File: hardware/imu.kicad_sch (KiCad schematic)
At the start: 0 parts

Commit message: wip: schematic sheets in progress
Co-Authored-By: Claude Opus 5.5 <noreply@anthropic.com>
Claude-Session: https://claude.ai/code/session_01RFaS5jnC9tnPam9GBgmGnG
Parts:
- added C61, C62: 1uF, lib:C_0201_0603Metric_W, symbol Device:C
- added R49: 10k, lib:R_0201_0603Metric_W, symbol Device:R
- added U11: BMI270, lib:LGA-14_L3.0-W2.5-P0.50-BR_W, symbol OpenDrone:BMI270
- added U12: TPS7A2018, lib:X2SON-4_L1.0-W1.0-P0.65-TL-EP_Dense, symbol lib:TPS7A2018PDQN
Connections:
- new net +1V8: C62.1, U11.8 (VDD), U12.1 (OUT)
- new net +3V3: C61.1, R49.2, U11.5 (VDDIO), U12.3 (EN), U12.4 (IN)
- new net GND: C61.2, C62.2, U11.6 (GNDIO), U11.7 (GND), U12.2 (GND), U12.5 (EP)
- new net GYRO_CLKIN: U11.9 (INT2)
- new net GYRO_CS: R49.1, U11.12 (CSB)
- new net GYRO_INT: U11.4 (INT1)
- new net SPI1_MISO: U11.1 (SDO)
- new net SPI1_MOSI: U11.14 (SDx)
- new net SPI1_SCK: U11.13 (SCx)
- no-connect marks 0 -> 4
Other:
- note added: "Universal IMU wiring and LGA-14 land (BMI270, ICM-42688-P)"

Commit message: wip: schematic integration in progress (saved after container restart)
Co-Authored-By: Claude Opus 5.5 <noreply@anthropic.com>
Claude-Session: https://claude.ai/code/session_01RFaS5jnC9tnPam9GBgmGnG
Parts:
- U11: symbol OpenDrone:BMI270 -> lib:BMI270
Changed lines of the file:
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@@
 		(in_pos_files no)
 		(dnp no)
-		(property "Reference" "#PWR01"
+		(property "Reference" "#PWR130"
 			(at 83.82 46.99 0)
 			(hide yes)
@@
 			(project "OpenAIO-Whoop"
 				(path "/2c3a7206-1e66-4d43-a02f-491225e20dd6/f446158c-b285-51eb-bc17-5ec1fb190fc1"
-					(reference "#PWR01")
+					(reference "#PWR130")
 					(unit 1)
 				)
@@
 		(in_pos_files no)
 		(dnp no)
-		(property "Reference" "#PWR07"
+		(property "Reference" "#PWR128"
 			(at 26.67 46.99 0)
 			(hide yes)
@@
 			(project "OpenAIO-Whoop"
 				(path "/2c3a7206-1e66-4d43-a02f-491225e20dd6/f446158c-b285-51eb-bc17-5ec1fb190fc1"
-					(reference "#PWR07")
+					(reference "#PWR128")
 					(unit 1)
 				)
@@
 	)
 	(symbol
-		(lib_id "OpenDrone:BMI270")
+		(lib_id "lib:BMI270")
 		(at 72.39 69.85 0)
 		(unit 1)
@@
 		(in_pos_files no)
 		(dnp no)
-		(property "Reference" "#PWR08"
+		(property "Reference" "#PWR133"
 			(at 41.91 62.23 0)
 			(hide yes)
@@
 			(project "OpenAIO-Whoop"
 				(path "/2c3a7206-1e66-4d43-a02f-491225e20dd6/f446158c-b285-51eb-bc17-5ec1fb190fc1"
-					(reference "#PWR08")
+					(reference "#PWR133")
 					(unit 1)
 				)
@@
 		(in_pos_files no)
 		(dnp no)
-		(property "Reference" "#PWR05"
+		(property "Reference" "#PWR135"
 			(at 72.39 99.06 0)
 			(hide yes)
@@
 			(project "OpenAIO-Whoop"
 				(path "/2c3a7206-1e66-4d43-a02f-491225e20dd6/f446158c-b285-51eb-bc17-5ec1fb190fc1"
-					(reference "#PWR05")
+					(reference "#PWR135")
 					(unit 1)
 				)
@@
 		(in_pos_files no)
 		(dnp no)
-		(property "Reference" "#PWR02"
+		(property "Reference" "#PWR132"
 			(at 83.82 57.15 0)
 			(hide yes)
@@
 			(project "OpenAIO-Whoop"
 				(path "/2c3a7206-1e66-4d43-a02f-491225e20dd6/f446158c-b285-51eb-bc17-5ec1fb190fc1"
-					(reference "#PWR02")
+					(reference "#PWR132")
 					(unit 1)
 				)
@@
 		(in_pos_files no)
 		(dnp no)
-		(property "Reference" "#PWR04"
+		(property "Reference" "#PWR131"
 			(at 62.23 57.15 0)
 			(hide yes)
@@
 			(project "OpenAIO-Whoop"
 				(path "/2c3a7206-1e66-4d43-a02f-491225e20dd6/f446158c-b285-51eb-bc17-5ec1fb190fc1"
-					(reference "#PWR04")
+					(reference "#PWR131")
 					(unit 1)
 				)
@@
 		(in_pos_files no)
 		(dnp no)
-		(property "Reference" "#PWR06"
+		(property "Reference" "#PWR134"
 			(at 116.84 82.55 0)
 			(hide yes)
@@
 			(project "OpenAIO-Whoop"
 				(path "/2c3a7206-1e66-4d43-a02f-491225e20dd6/f446158c-b285-51eb-bc17-5ec1fb190fc1"
-					(reference "#PWR06")
+					(reference "#PWR134")
 					(unit 1)
 				)
@@
 		(in_pos_files no)
 		(dnp no)
-		(property "Reference" "#PWR03"
+		(property "Reference" "#PWR129"
 			(at 62.23 46.99 0)
 			(hide yes)
@@
 			(project "OpenAIO-Whoop"
 				(path "/2c3a7206-1e66-4d43-a02f-491225e20dd6/f446158c-b285-51eb-bc17-5ec1fb190fc1"
-					(reference "#PWR03")
-					(unit 1)
-				)
+					(reference "#PWR129")
+					(unit 1)
+				)

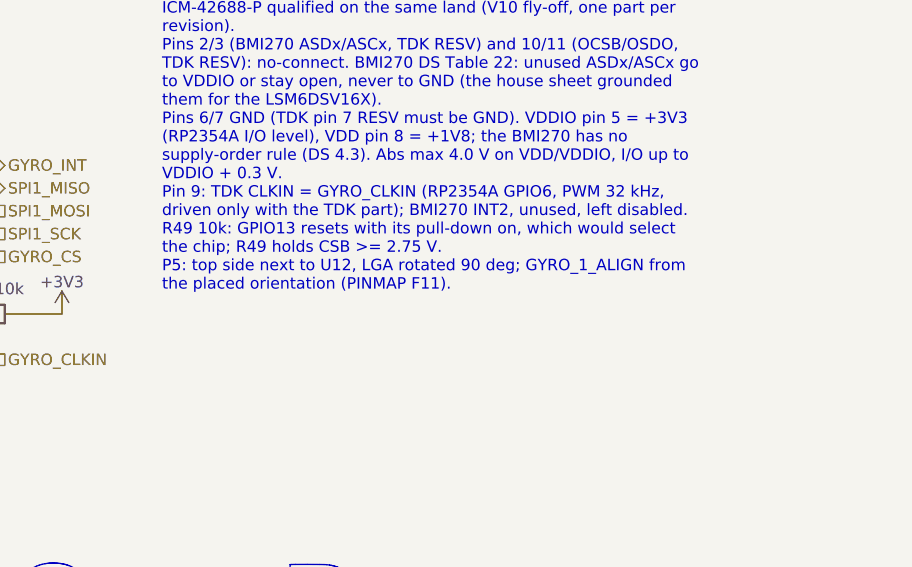
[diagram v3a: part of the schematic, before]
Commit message: wip: routing prep (zones and via fields) and schematic review round 4
Co-Authored-By: Claude Opus 5.5 <noreply@anthropic.com>
Claude-Session: https://claude.ai/code/session_01RFaS5jnC9tnPam9GBgmGnG
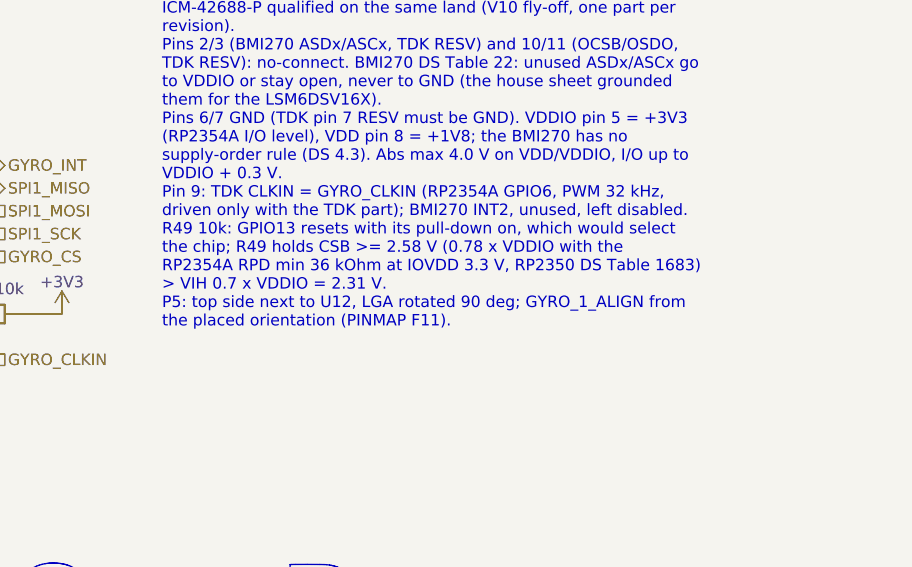
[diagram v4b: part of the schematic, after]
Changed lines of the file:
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@@
 		)
 	)
-	(text_box "GYRO BMI270: U11, R49\nSource: OpenFC-Lite-Mini imu.kicad_sch (universal LGA-14 land, SPI1 4-wire, R49), copied and adapted. BMI270 on the BOM; TDK ICM-42688-P qualified on the same land (V10 fly-off, one part per revision).\nPins 2/3 (BMI270 ASDx/ASCx, TDK RESV) and 10/11 (OCSB/OSDO, TDK RESV): no-connect. BMI270 DS Table 22: unused ASDx/ASCx go to VDDIO or stay open, never to GND (the house sheet grounded them for the LSM6DSV16X).\nPins 6/7 GND (TDK pin 7 RESV must be GND). VDDIO pin 5 = +3V3 (RP2354A I/O level), VDD pin 8 = +1V8; the BMI270 has no supply-order rule (DS 4.3). Abs max 4.0 V on VDD/VDDIO, I/O up to VDDIO + 0.3 V.\nPin 9: TDK CLKIN = GYRO_CLKIN (RP2354A GPIO6, PWM 32 kHz, driven only with the TDK part); BMI270 INT2, unused, left disabled.\nR49 10k: GPIO13 resets with its pull-down on, which would select the chip; R49 holds CSB >= 2.75 V.\nP5: top side next to U12, LGA rotated 90 deg; GYRO_1_ALIGN from the placed orientation (PINMAP F11)."
+	(text_box "GYRO BMI270: U11, R49\nSource: OpenFC-Lite-Mini imu.kicad_sch (universal LGA-14 land, SPI1 4-wire, R49), copied and adapted. BMI270 on the BOM; TDK ICM-42688-P qualified on the same land (V10 fly-off, one part per revision).\nPins 2/3 (BMI270 ASDx/ASCx, TDK RESV) and 10/11 (OCSB/OSDO, TDK RESV): no-connect. BMI270 DS Table 22: unused ASDx/ASCx go to VDDIO or stay open, never to GND (the house sheet grounded them for the LSM6DSV16X).\nPins 6/7 GND (TDK pin 7 RESV must be GND). VDDIO pin 5 = +3V3 (RP2354A I/O level), VDD pin 8 = +1V8; the BMI270 has no supply-order rule (DS 4.3). Abs max 4.0 V on VDD/VDDIO, I/O up to VDDIO + 0.3 V.\nPin 9: TDK CLKIN = GYRO_CLKIN (RP2354A GPIO6, PWM 32 kHz, driven only with the TDK part); BMI270 INT2, unused, left disabled.\nR49 10k: GPIO13 resets with its pull-down on, which would select the chip; R49 holds CSB >= 2.58 V (0.78 x VDDIO with the RP2354A RPD min 36 kOhm at IOVDD 3.3 V, RP2350 DS Table 1683) > VIH 0.7 x VDDIO = 2.31 V.\nP5: top side next to U12, LGA rotated 90 deg; GYRO_1_ALIGN from the placed orientation (PINMAP F11)."
 		(exclude_from_sim no)
 		(at 127 36.83 0)

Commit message: WIP final schematic (D111/D113): GPIO map, D100 oscillator, final footprints, lineup power-net names; mid-run snapshot, not yet verified (ERC/netlist/DRU regen pending)
Co-Authored-By: Claude Opus 5.5 <noreply@anthropic.com>
Claude-Session: https://claude.ai/code/session_01RFaS5jnC9tnPam9GBgmGnG
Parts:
- C61, C62: footprint lib:C_0201_0603Metric_W -> lib:C_0201_0603Metric_L
- R49: footprint lib:R_0201_0603Metric_W -> lib:R_0201_0603Metric_L
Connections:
- net +1V8 renamed +1.8V_GYRO
- net +3V3 renamed +3.3V
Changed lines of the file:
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@@
 		)
 	)
-	(text_box "GYRO BMI270: U11, R49\nSource: OpenFC-Lite-Mini imu.kicad_sch (universal LGA-14 land, SPI1 4-wire, R49), copied and adapted. BMI270 on the BOM; TDK ICM-42688-P qualified on the same land (V10 fly-off, one part per revision).\nPins 2/3 (BMI270 ASDx/ASCx, TDK RESV) and 10/11 (OCSB/OSDO, TDK RESV): no-connect. BMI270 DS Table 22: unused ASDx/ASCx go to VDDIO or stay open, never to GND (the house sheet grounded them for the LSM6DSV16X).\nPins 6/7 GND (TDK pin 7 RESV must be GND). VDDIO pin 5 = +3V3 (RP2354A I/O level), VDD pin 8 = +1V8; the BMI270 has no supply-order rule (DS 4.3). Abs max 4.0 V on VDD/VDDIO, I/O up to VDDIO + 0.3 V.\nPin 9: TDK CLKIN = GYRO_CLKIN (RP2354A GPIO6, PWM 32 kHz, driven only with the TDK part); BMI270 INT2, unused, left disabled.\nR49 10k: GPIO13 resets with its pull-down on, which would select the chip; R49 holds CSB >= 2.58 V (0.78 x VDDIO with the RP2354A RPD min 36 kOhm at IOVDD 3.3 V, RP2350 DS Table 1683) > VIH 0.7 x VDDIO = 2.31 V.\nP5: top side next to U12, LGA rotated 90 deg; GYRO_1_ALIGN from the placed orientation (PINMAP F11)."
+	(text_box "GYRO BMI270: U11, R49\nSource: OpenFC-Lite-Mini imu.kicad_sch (universal LGA-14 land, SPI1 4-wire, R49), copied and adapted. BMI270 on the BOM; TDK ICM-42688-P qualified on the same land (V10 fly-off, one part per revision).\nPins 2/3 (BMI270 ASDx/ASCx, TDK RESV) and 10/11 (OCSB/OSDO, TDK RESV): no-connect. BMI270 DS Table 22: unused ASDx/ASCx go to VDDIO or stay open, never to GND (the house sheet grounded them for the LSM6DSV16X).\nPins 6/7 GND (TDK pin 7 RESV must be GND). VDDIO pin 5 = +3.3V (RP2354A I/O level), VDD pin 8 = +1.8V_GYRO; the BMI270 has no supply-order rule (DS 4.3). Abs max 4.0 V on VDD/VDDIO, I/O up to VDDIO + 0.3 V.\nPin 9: TDK CLKIN = GYRO_CLKIN (RP2354A GPIO6, PWM 32 kHz, driven only with the TDK part); BMI270 INT2, unused, left disabled.\nR49 10k: GPIO13 resets with its pull-down on, which would select the chip; R49 holds CSB >= 2.58 V (0.78 x VDDIO with the RP2354A RPD min 36 kOhm at IOVDD 3.3 V, RP2350 DS Table 1683) > VIH 0.7 x VDDIO = 2.31 V.\nP5: top side next to U12, LGA rotated 90 deg; GYRO_1_ALIGN from the placed orientation (PINMAP F11)."
 		(exclude_from_sim no)
 		(at 127 36.83 0)
@@
 		)
 	)
-	(text_box "+1V8 GYRO LDO: U12, C61, C62 (D52 BR-09, P4-17)\nSource: pcb-agent-commons blocks/LDO_IMU_TPS7A2033 (OpenFC-H7) topology with the 1.8 V part and no ferrite (fed from the +3V3 LDO); the house OpenFC-Lite-Mini also runs the gyro VDD from its own 1.8 V LDO.\nTPS7A2018 DQN: 1 OUT, 2 GND, 3 EN, 4 IN, 5 EP to GND. IN = EN = +3V3: VIN 1.6-6.0 V, VEN 0-6.0 V (abs max 6.5 V), EN never above IN. Load < 1 mA.\nNo 100 nF at the gyro: C61 = U12 CIN at BMI270 VDDIO pin 5, C62 = U12 COUT at VDD pin 8 (COUT >= 0.47 uF effective, ESR <= 100 mOhm: about 0.6-0.85 uF at 1.8 V). C61 counts in the +3V3 COUT sum (P4-12, POWER).\nP5: U12 on the gyro side with OUT facing pin 8; C61 between U12 pin 4 and gyro pin 5, C62 <= 1.5 mm from pin 8 (PS-06), else re-place U12."
+	(text_box "+1.8V_GYRO GYRO LDO: U12, C61, C62 (D52 BR-09, P4-17)\nSource: pcb-agent-commons blocks/LDO_IMU_TPS7A2033 (OpenFC-H7) topology with the 1.8 V part and no ferrite (fed from the +3.3V LDO); the house OpenFC-Lite-Mini also runs the gyro VDD from its own 1.8 V LDO.\nTPS7A2018 DQN: 1 OUT, 2 GND, 3 EN, 4 IN, 5 EP to GND. IN = EN = +3.3V: VIN 1.6-6.0 V, VEN 0-6.0 V (abs max 6.5 V), EN never above IN. Load < 1 mA.\nNo 100 nF at the gyro: C61 = U12 CIN at BMI270 VDDIO pin 5, C62 = U12 COUT at VDD pin 8 (COUT >= 0.47 uF effective, ESR <= 100 mOhm: about 0.6-0.85 uF at 1.8 V). C61 counts in the +3.3V COUT sum (P4-12, POWER).\nP5: U12 on the gyro side with OUT facing pin 8; C61 between U12 pin 4 and gyro pin 5, C62 <= 1.5 mm from pin 8 (PS-06), else re-place U12."
 		(exclude_from_sim no)
 		(at 12.7 99.06 0)
@@
 	)
 	(symbol
-		(lib_id "power:+3V3")
+		(lib_id "power:+3.3V")
 		(at 83.82 43.18 0)
 		(unit 1)
@@
 		(in_pos_files no)
 		(dnp no)
-		(property "Reference" "#PWR135"
+		(property "Reference" "#PWR136"
 			(at 83.82 46.99 0)
 			(hide yes)
@@
 			)
 		)
-		(property "Value" "+3V3"
+		(property "Value" "+3.3V"
 			(at 83.82 39.624 0)
 			(show_name no)
@@
 			)
 		)
-		(property "Description" "Power symbol creates a global label with name \"+3V3\""
+		(property "Description" "Power symbol creates a global label with name \"+3.3V\""
 			(at 83.82 43.18 0)
 			(hide yes)
@@
 			(project "OpenAIO-Whoop"
 				(path "/2c3a7206-1e66-4d43-a02f-491225e20dd6/f446158c-b285-51eb-bc17-5ec1fb190fc1"
-					(reference "#PWR135")
+					(reference "#PWR136")
 					(unit 1)
 				)
@@
 	)
 	(symbol
-		(lib_id "power:+3V3")
+		(lib_id "power:+3.3V")
 		(at 26.67 43.18 0)
 		(unit 1)
@@
 		(in_pos_files no)
 		(dnp no)
-		(property "Reference" "#PWR133"
+		(property "Reference" "#PWR134"
 			(at 26.67 46.99 0)
 			(hide yes)
@@
 			)
 		)
-		(property "Value" "+3V3"
+		(property "Value" "+3.3V"
 			(at 26.67 39.624 0)
 			(show_name no)
@@
 			)
 		)
-		(property "Description" "Power symbol creates a global label with name \"+3V3\""
+		(property "Description" "Power symbol creates a global label with name \"+3.3V\""
 			(at 26.67 43.18 0)
 			(hide yes)
@@
 			(project "OpenAIO-Whoop"
 				(path "/2c3a7206-1e66-4d43-a02f-491225e20dd6/f446158c-b285-51eb-bc17-5ec1fb190fc1"
-					(reference "#PWR133")
+					(reference "#PWR134")
 					(unit 1)
 				)
@@
 			)
 		)
-		(property "Footprint" "lib:C_0201_0603Metric_W"
+		(property "Footprint" "lib:C_0201_0603Metric_L"
 			(at 62.23 46.99 0)
 			(hide yes)
@@
 			)
 		)
-		(property "Footprint" "lib:C_0201_0603Metric_W"
+		(property "Footprint" "lib:C_0201_0603Metric_L"
 			(at 83.82 46.99 0)
 			(hide yes)
@@
 		(in_pos_files no)
 		(dnp no)
-		(property "Reference" "#PWR138"
+		(property "Reference" "#PWR139"
 			(at 41.91 62.23 0)
 			(hide yes)
@@
 			(project "OpenAIO-Whoop"
 				(path "/2c3a7206-1e66-4d43-a02f-491225e20dd6/f446158c-b285-51eb-bc17-5ec1fb190fc1"
-					(reference "#PWR138")
+					(reference "#PWR139")
 					(unit 1)
 				)
@@
 		(in_pos_files no)
 		(dnp no)
-		(property "Reference" "#PWR140"
+		(property "Reference" "#PWR141"
 			(at 72.39 99.06 0)
 			(hide yes)
@@
 			(project "OpenAIO-Whoop"
 				(path "/2c3a7206-1e66-4d43-a02f-491225e20dd6/f446158c-b285-51eb-bc17-5ec1fb190fc1"
-					(reference "#PWR140")
+					(reference "#PWR141")
 					(unit 1)
 				)
@@
 		(in_pos_files no)
 		(dnp no)
-		(property "Reference" "#PWR137"
+		(property "Reference" "#PWR138"
 			(at 83.82 57.15 0)
 			(hide yes)
@@
 			(project "OpenAIO-Whoop"
 				(path "/2c3a7206-1e66-4d43-a02f-491225e20dd6/f446158c-b285-51eb-bc17-5ec1fb190fc1"
-					(reference "#PWR137")
+					(reference "#PWR138")
 					(unit 1)
 				)
@@
 		(in_pos_files no)
 		(dnp no)
-		(property "Reference" "#PWR136"
+		(property "Reference" "#PWR137"
 			(at 62.23 57.15 0)
 			(hide yes)
@@
 			(project "OpenAIO-Whoop"
 				(path "/2c3a7206-1e66-4d43-a02f-491225e20dd6/f446158c-b285-51eb-bc17-5ec1fb190fc1"
-					(reference "#PWR136")
+					(reference "#PWR137")
 					(unit 1)
 				)
@@
 	)
 	(symbol
-		(lib_id "power:+3V3")
+		(lib_id "power:+3.3V")
 		(at 116.84 78.74 0)
 		(unit 1)
@@
 		(in_pos_files no)
 		(dnp no)
-		(property "Reference" "#PWR139"
+		(property "Reference" "#PWR140"
 			(at 116.84 82.55 0)
 			(hide yes)
@@
 			)
 		)
-		(property "Value" "+3V3"
+		(property "Value" "+3.3V"
 			(at 116.84 75.184 0)
 			(show_name no)
@@
 			)
 		)
-		(property "Description" "Power symbol creates a global label with name \"+3V3\""
+		(property "Description" "Power symbol creates a global label with name \"+3.3V\""
 			(at 116.84 78.74 0)
 			(hide yes)
@@
 			(project "OpenAIO-Whoop"
 				(path "/2c3a7206-1e66-4d43-a02f-491225e20dd6/f446158c-b285-51eb-bc17-5ec1fb190fc1"
-					(reference "#PWR139")
+					(reference "#PWR140")
 					(unit 1)
 				)
@@
 			)
 		)
-		(property "Footprint" "lib:R_0201_0603Metric_W"
+		(property "Footprint" "lib:R_0201_0603Metric_L"
 			(at 107.95 78.74 0)
 			(hide yes)
@@
 	)
 	(symbol
-		(lib_id "power:+1V8")
+		(lib_id "power:+3.3V")
 		(at 62.23 43.18 0)
 		(unit 1)
@@
 		(in_pos_files no)
 		(dnp no)
-		(property "Reference" "#PWR134"
+		(property "Reference" "#PWR135"
 			(at 62.23 46.99 0)
 			(hide yes)
@@
 			)
 		)
-		(property "Value" "+1V8"
+		(property "Value" "+1.8V_GYRO"
 			(at 62.23 39.624 0)
 			(show_name no)
@@
 			)
 		)
-		(property "Description" "Power symbol creates a global label with name \"+1V8\""
+		(property "Description" "Power symbol creates a global label with name \"+1.8V_GYRO\""
 			(at 62.23 43.18 0)
 			(hide yes)
@@
 			(project "OpenAIO-Whoop"
 				(path "/2c3a7206-1e66-4d43-a02f-491225e20dd6/f446158c-b285-51eb-bc17-5ec1fb190fc1"
-					(reference "#PWR134")
+					(reference "#PWR135")
 					(unit 1)
 				)

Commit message: WIP final schematic (D111/D113): further sheet and doc updates, PDF re-export; mid-run snapshot, not yet verified
Co-Authored-By: Claude Opus 5.5 <noreply@anthropic.com>
Claude-Session: https://claude.ai/code/session_01RFaS5jnC9tnPam9GBgmGnG
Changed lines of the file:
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@@
 		)
 	)
-	(text_box "GYRO BMI270: U11, R49\nSource: OpenFC-Lite-Mini imu.kicad_sch (universal LGA-14 land, SPI1 4-wire, R49), copied and adapted. BMI270 on the BOM; TDK ICM-42688-P qualified on the same land (V10 fly-off, one part per revision).\nPins 2/3 (BMI270 ASDx/ASCx, TDK RESV) and 10/11 (OCSB/OSDO, TDK RESV): no-connect. BMI270 DS Table 22: unused ASDx/ASCx go to VDDIO or stay open, never to GND (the house sheet grounded them for the LSM6DSV16X).\nPins 6/7 GND (TDK pin 7 RESV must be GND). VDDIO pin 5 = +3.3V (RP2354A I/O level), VDD pin 8 = +1.8V_GYRO; the BMI270 has no supply-order rule (DS 4.3). Abs max 4.0 V on VDD/VDDIO, I/O up to VDDIO + 0.3 V.\nPin 9: TDK CLKIN = GYRO_CLKIN (RP2354A GPIO6, PWM 32 kHz, driven only with the TDK part); BMI270 INT2, unused, left disabled.\nR49 10k: GPIO13 resets with its pull-down on, which would select the chip; R49 holds CSB >= 2.58 V (0.78 x VDDIO with the RP2354A RPD min 36 kOhm at IOVDD 3.3 V, RP2350 DS Table 1683) > VIH 0.7 x VDDIO = 2.31 V.\nP5: top side next to U12, LGA rotated 90 deg; GYRO_1_ALIGN from the placed orientation (PINMAP F11)."
+	(text_box "GYRO BMI270: U11, R49\nSource: OpenFC-Lite-Mini imu.kicad_sch (universal LGA-14 land, SPI1 4-wire, R49), copied and adapted. BMI270 on the BOM; TDK ICM-42688-P qualified on the same land (V10 fly-off, one part per revision).\nPins 2/3 (BMI270 ASDx/ASCx, TDK RESV) and 10/11 (OCSB/OSDO, TDK RESV): no-connect. BMI270 DS Table 22: unused ASDx/ASCx go to VDDIO or stay open, never to GND (the house sheet grounded them for the LSM6DSV16X).\nPins 6/7 GND (TDK pin 7 RESV must be GND). VDDIO pin 5 = +3.3V (RP2354A I/O level), VDD pin 8 = +1.8V_GYRO; the BMI270 has no supply-order rule (DS 4.3). Abs max 4.0 V on VDD/VDDIO, I/O up to VDDIO + 0.3 V.\nPin 9: TDK CLKIN = GYRO_CLKIN (RP2354A GPIO13, PWM 32 kHz, driven only with the TDK part); BMI270 INT2, unused, left disabled.\nR49 10k: GYRO_CS (GPIO15) resets with its pull-down on, which would select the chip; R49 holds CSB >= 2.58 V (0.78 x VDDIO with the RP2354A RPD min 36 kOhm at IOVDD 3.3 V, RP2350 DS Table 1683) > VIH 0.7 x VDDIO = 2.31 V.\nP5: top side next to U12, LGA rotated 90 deg; GYRO_1_ALIGN from the placed orientation (PINMAP F11)."
 		(exclude_from_sim no)
 		(at 127 36.83 0)
